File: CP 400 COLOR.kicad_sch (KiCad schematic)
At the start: 154 parts, among them CN1 CN9, CN10 CN10, CN13 CN13, CN14 CN14, CN2 CASSETE, CN3 CN8, CN4 RS232, CN5 JOYESQ, CN6 JOYDIR, CN7 CP400_CN7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

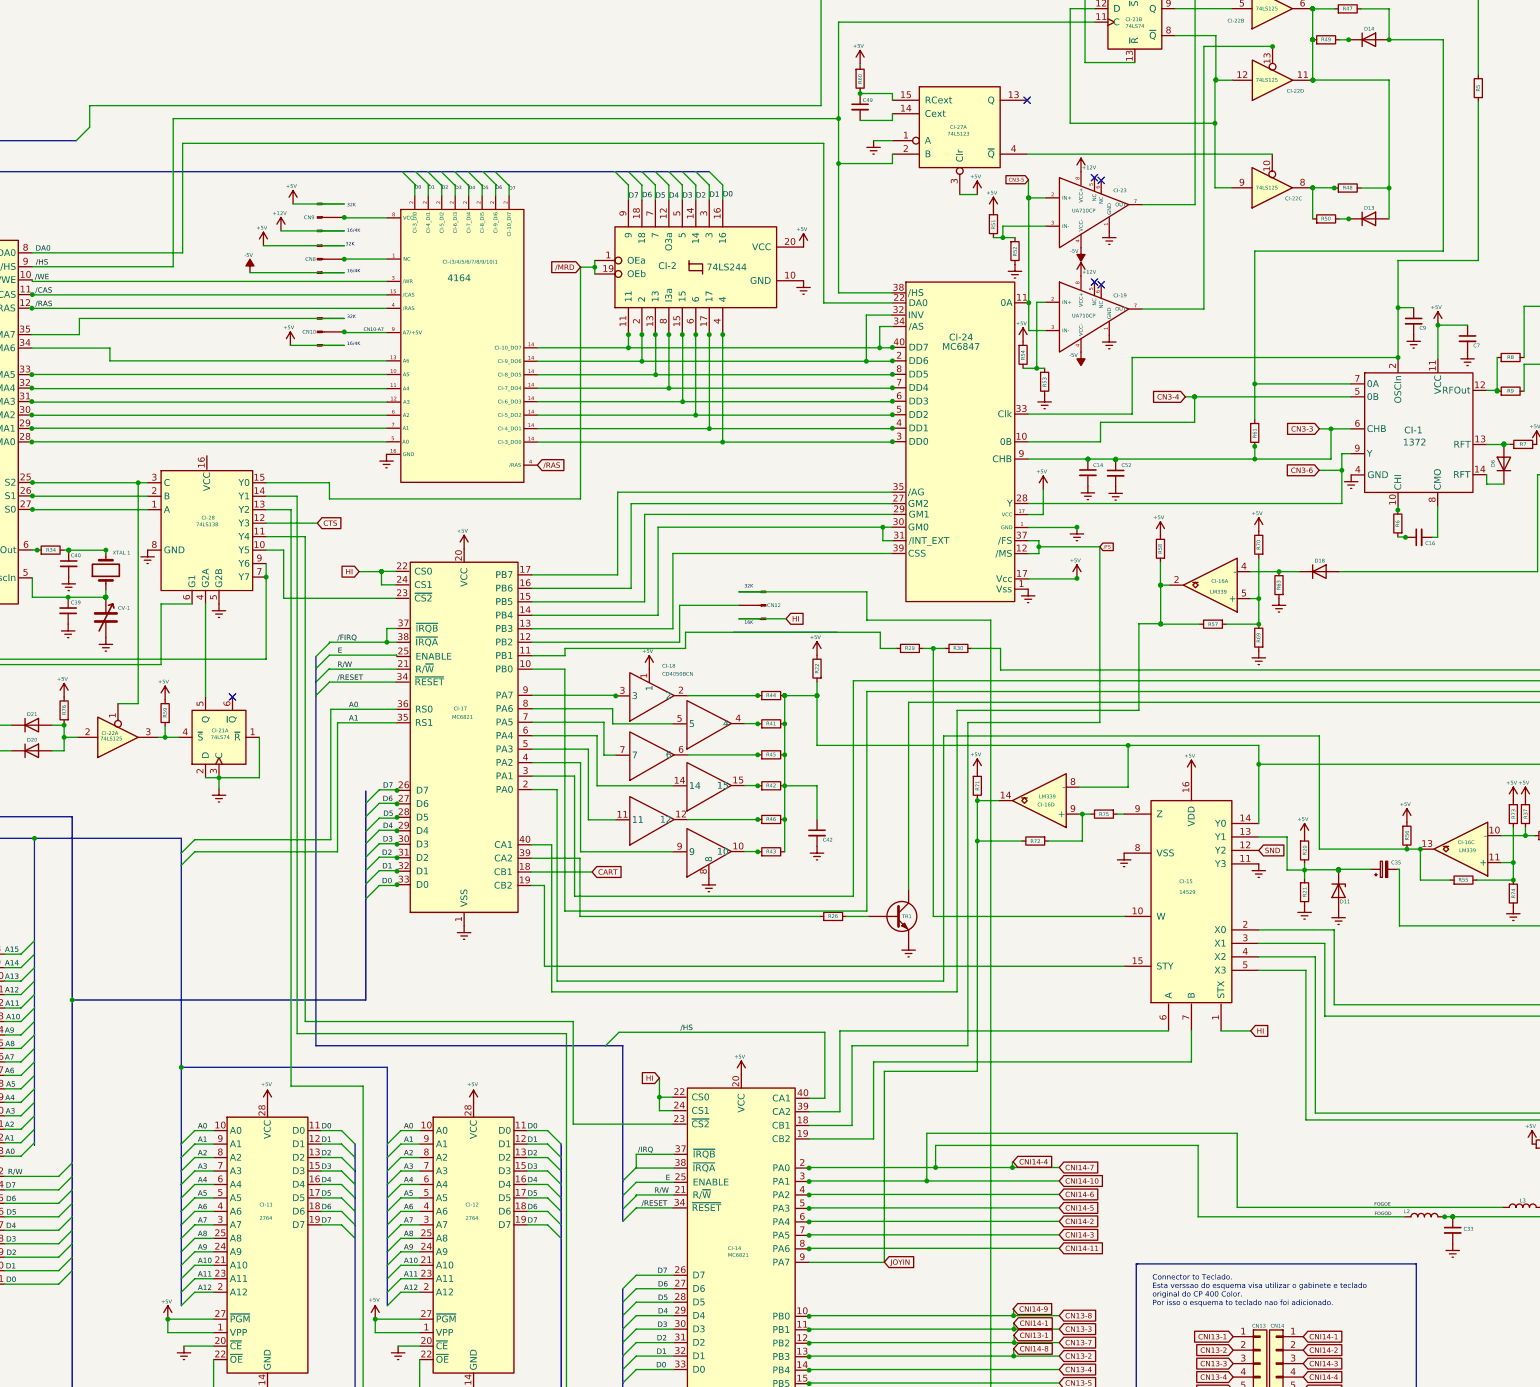
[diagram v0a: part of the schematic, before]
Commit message: Fixed VCLK signal not connected to MC1372P
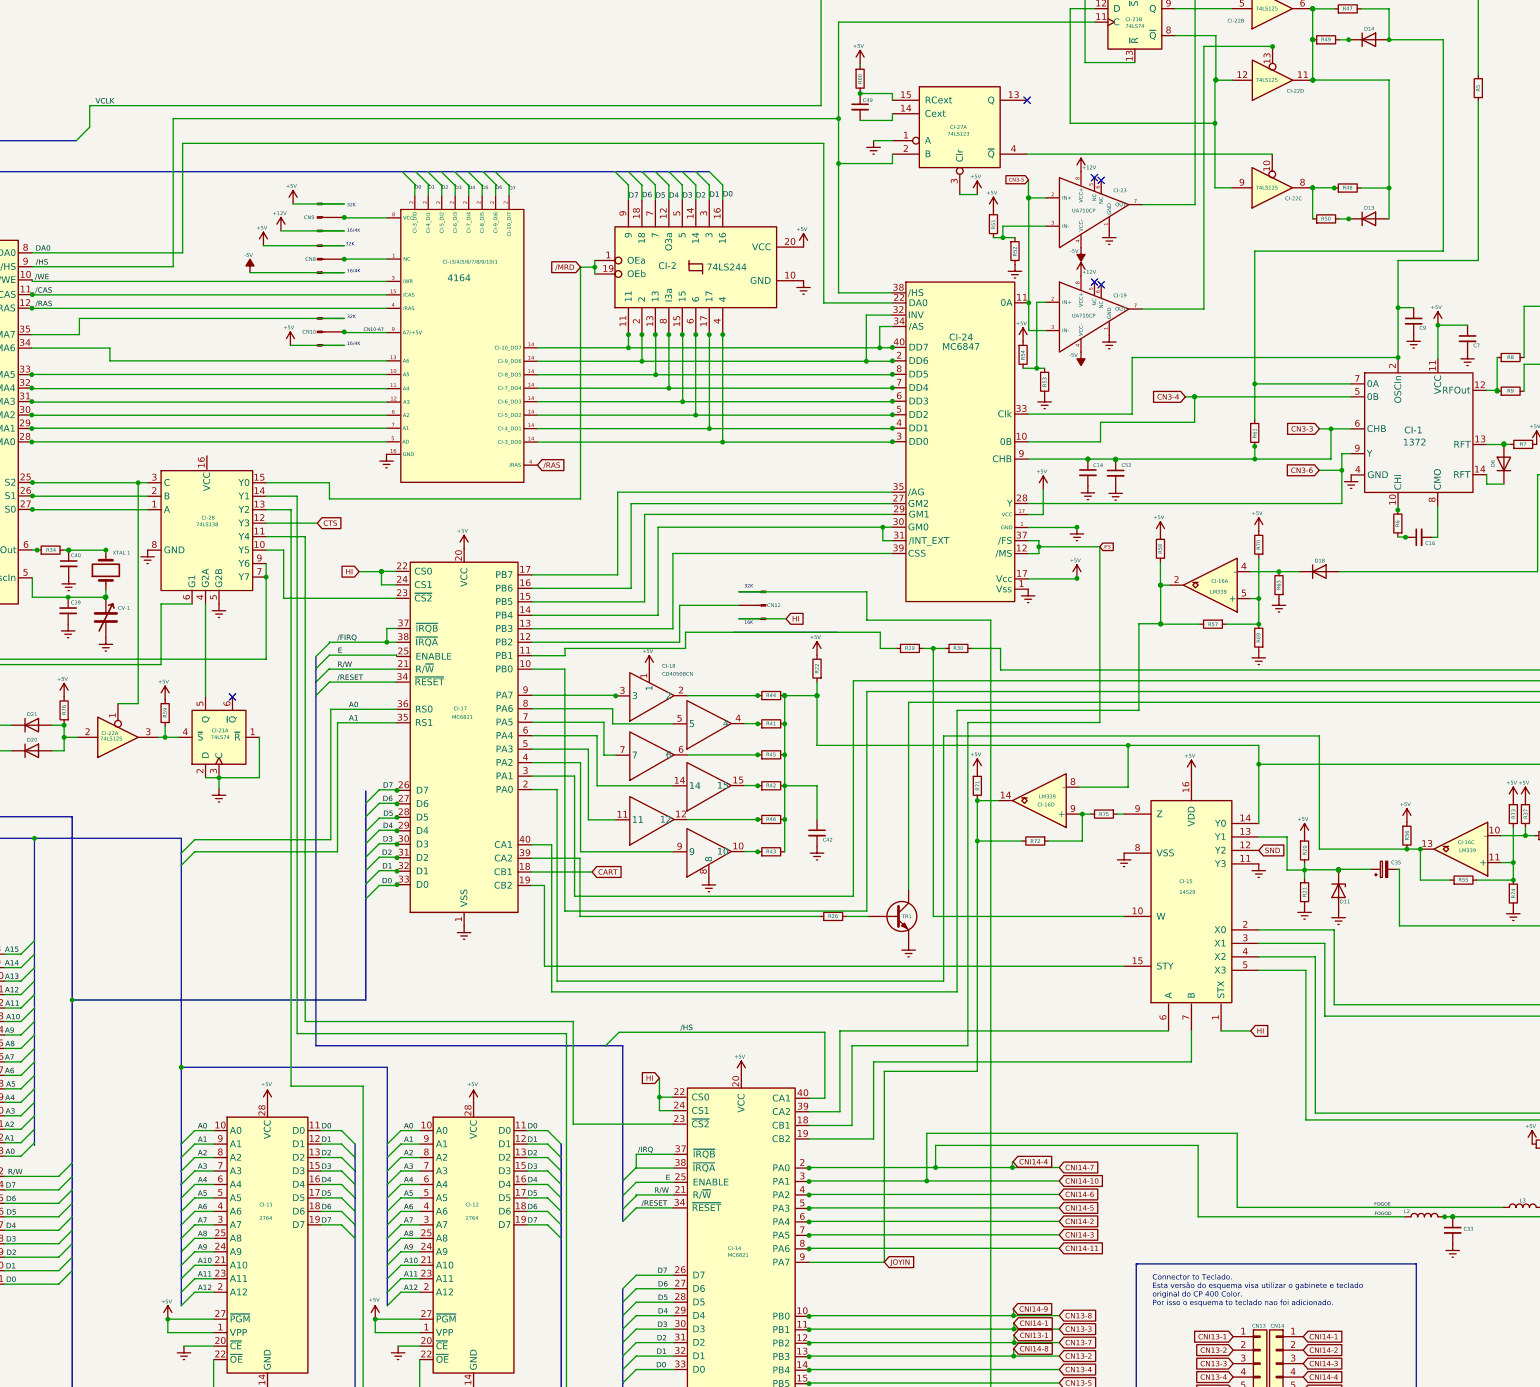
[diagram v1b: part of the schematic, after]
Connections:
- net VCLK: now also R5.2
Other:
- note added: "Connector to Teclado. Esta versão do esquema visa utilizar o gabinete e teclado original do CP 400 Color. Por isso o esquema to teclado nao foi adicionado."
- note removed: "Connector to Teclado. Esta verssao do esquema visa utilizar o gabinete e teclado original do CP 400 Color. Por isso o esquema to teclado nao foi adicionado."
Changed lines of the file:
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@@
   (title_block
     (title "CP 400 COLOR 2 - PROLOGICA 12 REV.3")
-    (date "2022-12-09")
+    (date "2022-12-13")
     (rev "0.3")
     (company "PROLOGICA")
@@
     (effects (font (size 0.635 0.635)) (justify left bottom))
   )
-  (text "Connector to Teclado.\nEsta verssao do esquema visa utilizar o gabinete e teclado \noriginal do CP 400 Color.\nPor isso o esquema to teclado nao foi adicionado."
+  (text "Connector to Teclado.\nEsta versão do esquema visa utilizar o gabinete e teclado \noriginal do CP 400 Color.\nPor isso o esquema to teclado nao foi adicionado."
     (at 359.918 279.4 0)
     (effects (font (size 1 1)) (justify left bottom))
@@
     (effects (font (size 1 1)) (justify left bottom))
   )
+  (label "VCLK" (at 160.5949 52.832 0)
+    (effects (font (size 1 1)) (justify left bottom))
+  )

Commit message: Added some component values, in what is promised to be a huge work ahead
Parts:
- removed C7: C7, Capacitor_THT:C_Disc_D3.0mm_W1.6mm_P2.50mm, symbol Device:C_Small
- added C7: 100uF, Capacitor_THT:CP_Radial_Tantal_D10.5mm_P5.00mm, symbol Device:C_Polarized_Small
- C15: value C16 -> 104
- C9: value C9 -> 560pF
- D6: value D6 -> 1N4002
- R5: value R5 -> 470
- R7: value R7 -> 360
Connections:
- net +5V: now also C7.1
- net GNDREF: now also C7.2

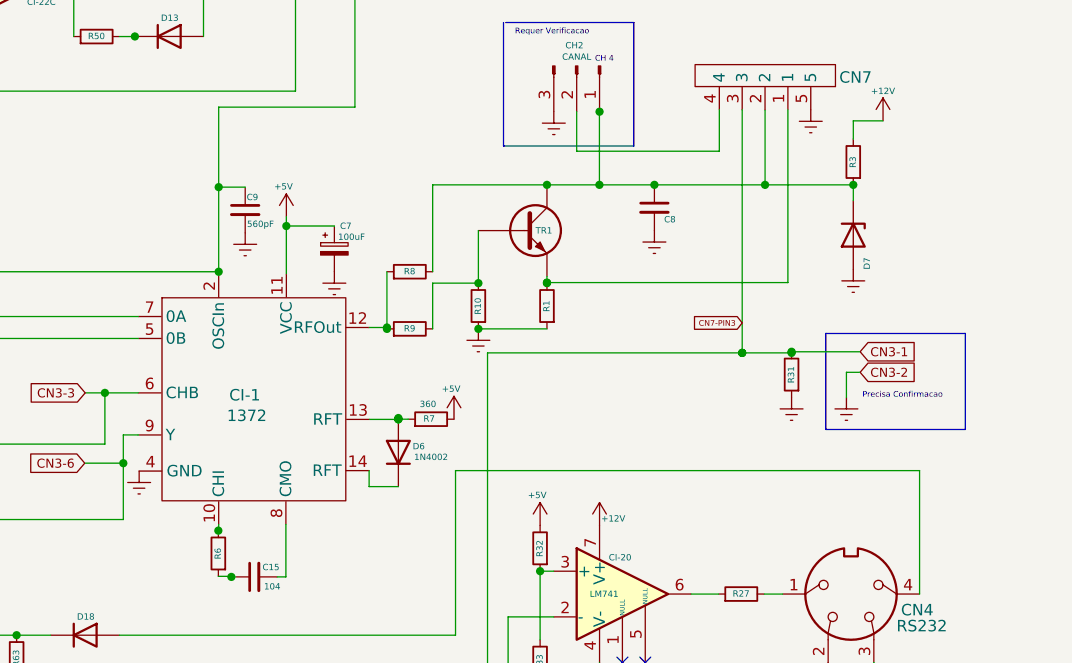
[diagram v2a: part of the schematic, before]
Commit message: Updates to some more component values; added an C8b that was not in the schematic
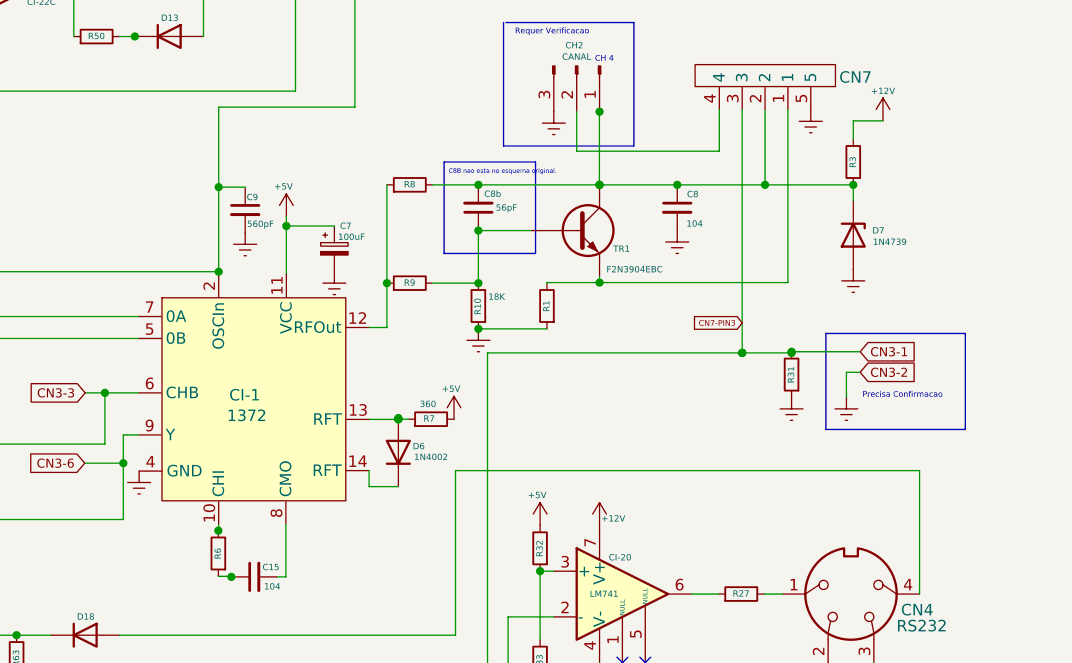
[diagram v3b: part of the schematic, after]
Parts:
- added C8b: 56pF, Capacitor_THT:C_Disc_D3.0mm_W1.6mm_P2.50mm, symbol Device:C_Small
- C8: value C8 -> 104
- D7: value D7 -> 1N4739
- R10: value R10 -> 18K
- TR1: value TR1 -> F2N3904EBC
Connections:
- net at C8.1, CH2.1 (Pin_1), CN7.2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: now also C8b.2
- net at R10.2, R9.2, TR1.2 (B): now also C8b.1
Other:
- note added: "C8B nao esta no esquema original."

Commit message: Added some components values; Added Photo with component identification in the PCB - WIP
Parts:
- C39: value C39 -> 220
- C40: value C40 -> 220
- C44: value C44 -> 1Uf 100V; footprint Capacitor_THT:CP_Radial_Tantal_D10.5mm_P5.00mm -> Capacitor_THT:CP_Axial_L10.0mm_D4.5mm_P15.00mm_Horizontal
- C45: value C45 -> 104
- C49: value C49 -> 152
- CI-(3/4/5/6/7/8/9/10)1: now left out of the parts list
- CI-23: footprint Package_DIP:DIP-8-N7_W7.62mm -> Package_DIP:DIP-8_W7.62mm
- D13: value D13 -> 1N4148
- D14: value D14 -> 1N4148
- D15: value D15 -> 1N4148
- D16: value D16 -> 1N4148
- D17: value D17 -> 1N4148
- D20: value D20 -> 1N4148
- D21: value D21 -> 1N4148
- R34: value R34 -> 1.5K
- R35: value R35 -> 100K
- R36: value R36 -> 100K
- R47: value R47 -> 9.1K 1%; footprint Resistor_THT:R_Axial_DIN0207_L6.3mm_D2.5mm_P7.62mm_Horizontal -> Resistor_THT:R_Axial_DIN0207_L6.3mm_D2.5mm_P5.08mm_Vertical
- R48: value R48 -> 7.5K; footprint Resistor_THT:R_Axial_DIN0207_L6.3mm_D2.5mm_P7.62mm_Horizontal -> Resistor_THT:R_Axial_DIN0207_L6.3mm_D2.5mm_P5.08mm_Vertical
- R49: value R49 -> 4.7K; footprint Resistor_THT:R_Axial_DIN0207_L6.3mm_D2.5mm_P7.62mm_Horizontal -> Resistor_THT:R_Axial_DIN0207_L6.3mm_D2.5mm_P5.08mm_Vertical
- R50: value R50 -> 1.2K; footprint Resistor_THT:R_Axial_DIN0207_L6.3mm_D2.5mm_P7.62mm_Horizontal -> Resistor_THT:R_Axial_DIN0207_L6.3mm_D2.5mm_P5.08mm_Vertical
- R51, R52, R53, R54: footprint Resistor_THT:R_Axial_DIN0207_L6.3mm_D2.5mm_P7.62mm_Horizontal -> Resistor_THT:R_Axial_DIN0207_L6.3mm_D2.5mm_P5.08mm_Vertical
- R59: value R59 -> 4.7K; footprint Resistor_THT:R_Axial_DIN0207_L6.3mm_D2.5mm_P7.62mm_Horizontal -> Resistor_THT:R_Axial_DIN0207_L6.3mm_D2.5mm_P5.08mm_Vertical
- R60: value R60 -> 3.3K; footprint Resistor_THT:R_Axial_DIN0207_L6.3mm_D2.5mm_P7.62mm_Horizontal -> Resistor_THT:R_Axial_DIN0207_L6.3mm_D2.5mm_P5.08mm_Vertical
- R76: value R76 -> 10K; footprint Resistor_THT:R_Axial_DIN0207_L6.3mm_D2.5mm_P7.62mm_Horizontal -> Resistor_THT:R_Axial_DIN0207_L6.3mm_D2.5mm_P5.08mm_Vertical
- XTAL1: value XTAL 1 -> 14,30244 Mhz
- renumbered C8b to C8b1
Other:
- note added: "R47 Precisa Confirmacao"

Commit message: Updated PCB component layout (photography)
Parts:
- added C10: 104, Capacitor_THT:C_Disc_D3.0mm_W1.6mm_P2.50mm, symbol Device:C_Small
- C1: value C1 -> 223
- C35: value C35 -> 10uf 25v
- C36: value C36 -> 222
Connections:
- net +5V: now also CI-28.16 (VCC), C10.1
- net GNDREF: now also C10.2
- net at C35.1, D11.1 (K): now also CI-15.13 (Y1), R20.2, R21.1
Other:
- note added: "Added in Rev 3"
- note added: "Removido no PCB Rev3"
- note added: "Reset Circuit"
- moved on the sheet: CI-27C

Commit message: .
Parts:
- R47: value 9.1K 1% -> R47
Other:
- note added: "C8b1 nao esta no esquema original."
- note removed: "C8B nao esta no esquema original."
- note removed: "R47 Precisa Confirmacao"
- moved on the sheet: CI-2
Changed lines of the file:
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@@
     (effects (font (size 0.635 0.635)) (justify left bottom))
   )
-  (text "RESET signal \nfrom Keyboard\n" (at 105.41 156.972 0)
+  (text "RESET signal \nfrom Keyboard\n" (at 106.68 157.226 0)
     (effects (font (size 0.635 0.635)) (justify left bottom))
   )
@@
     (effects (font (size 0.635 0.635)) (justify left bottom))
   )
-  (text "C8B nao esta no esquema original." (at 431.8 89.662 0)
+  (text "C8b1 nao esta no esquema original." (at 431.8 89.662 0)
     (effects (font (size 0.5 0.5)) (justify left bottom))
   )
@@
     (effects (font (size 0.635 0.635)) (justify left bottom))
   )
-  (text "R47\nPrecisa Confirmacao" (at 392.684 33.274 0)
-    (effects (font (size 0.635 0.635)) (justify left bottom))
-  )
   (text "Precisa Confirmacao" (at 477.774 114.554 0)
     (effects (font (size 0.635 0.635)) (justify left bottom))
@@
     (pin "3")
   )
-  (symbol (lib_id "power:GNDREF") (at 294.132 85.852 0) (unit 1)
+  (symbol (lib_id "power:GNDREF") (at 287.274 85.852 0) (unit 1)
     (in_bom yes) (on_board yes) (fields_autoplaced)
-    (property "Reference" "#PWR02" (id 0) (at 294.132 92.202 0)
+    (property "Reference" "#PWR02" (id 0) (at 287.274 92.202 0)
       (effects (font (size 0.7 0.7)) hide)
     )
-    (property "Value" "GNDREF" (id 1) (at 294.132 90.424 0)
+    (property "Value" "GNDREF" (id 1) (at 287.274 90.424 0)
       (effects (font (size 0.7 0.7)) hide)
     )
-    (property "Footprint" "" (id 2) (at 294.132 85.852 0)
+    (property "Footprint" "" (id 2) (at 287.274 85.852 0)
       (effects (font (size 0.7 0.7)) hide)
     )
-    (property "Datasheet" "" (id 3) (at 294.132 85.852 0)
+    (property "Datasheet" "" (id 3) (at 287.274 85.852 0)
       (effects (font (size 0.7 0.7)) hide)
     )
@@
       (effects (font (size 0.7 0.7)) (justify left))
     )
-    (property "Value" "9.1K 1%" (id 1) (at 396.748 36.068 90)
+    (property "Value" "R47" (id 1) (at 396.748 36.068 90)
       (effects (font (size 0.7 0.7)))
     )
@@
     (pin "7")
   )
-  (symbol (lib_id "power:+5V") (at 294.132 79.502 0) (unit 1)
+  (symbol (lib_id "power:+5V") (at 287.274 79.502 0) (unit 1)
     (in_bom yes) (on_board yes)
-    (property "Reference" "#PWR01" (id 0) (at 294.132 83.312 0)
+    (property "Reference" "#PWR01" (id 0) (at 287.274 83.312 0)
       (effects (font (size 0.7 0.7)) hide)
     )
-    (property "Value" "+5V" (id 1) (at 293.8145 76.1369 0)
+    (property "Value" "+5V" (id 1) (at 286.9565 76.1369 0)
       (effects (font (size 0.7 0.7)))
     )
-    (property "Footprint" "" (id 2) (at 294.132 79.502 0)
+    (property "Footprint" "" (id 2) (at 287.274 79.502 0)
       (effects (font (size 0.7 0.7)) hide)
     )
-    (property "Datasheet" "" (id 3) (at 294.132 79.502 0)
+    (property "Datasheet" "" (id 3) (at 287.274 79.502 0)
       (effects (font (size 0.7 0.7)) hide)
     )
@@
   (symbol (lib_id "Roni:CP400_74LS244") (at 273.812 83.312 90) (unit 1)
     (in_bom yes) (on_board yes)
-    (property "Reference" "CI-2" (id 0) (at 268.478 83.058 90))
-    (property "Value" "74LS244" (id 1) (at 279.654 83.312 90))
+    (property "Reference" "CI-2" (id 0) (at 269.494 81.534 90)
+      (effects (font (size 1 1)))
+    )
+    (property "Value" "74LS244" (id 1) (at 268.986 83.312 90)
+      (effects (font (size 1 1)))
+    )
     (property "Footprint" "Package_DIP:DIP-20_W7.62mm" (id 2) (at 273.812 83.312 0)
       (effects (font (size 1.27 1.27)) hide)
@@
     )
     (path "/293bb476-09a1-45bb-8b16-3248945a44ac"
-      (reference "R47") (unit 1) (value "9.1K 1%") (footprint "Resistor_THT:R_Axial_DIN0207_L6.3mm_D2.5mm_P5.08mm_Vertical")
+      (reference "R47") (unit 1) (value "R47") (footprint "Resistor_THT:R_Axial_DIN0207_L6.3mm_D2.5mm_P5.08mm_Vertical")
     )
     (path "/4f55b128-5cbf-46db-a25a-4ef4d3bb4758"

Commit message: .
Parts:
- C1, C10, C12, C13, C14, C15, C2, C3, C33, C34, C36, C39, C4, C40, C42, C45, C49, C5, C52, C6, C8, C8b1, C9: footprint Capacitor_THT:C_Disc_D3.0mm_W1.6mm_P2.50mm -> Capacitor_THT:C_Axial_L3.8mm_D2.6mm_P7.50mm_Horizontal
- D12, D13, D15, D16, D17, D18, D19, D20, D21: footprint Diode_THT:D_DO-34_SOD68_P10.16mm_Horizontal -> Diode_THT:D_DO-34_SOD68_P7.62mm_Horizontal
- D14: footprint Diode_THT:D_DO-34_SOD68_P10.16mm_Horizontal -> Diode_THT:D_DO-35_SOD27_P2.54mm_Vertical_AnodeUp
- R22, R41, R42, R43, R44, R45, R46: footprint Resistor_THT:R_Axial_DIN0207_L6.3mm_D2.5mm_P7.62mm_Horizontal -> Resistor_THT:R_Axial_DIN0207_L6.3mm_D2.5mm_P2.54mm_Vertical
- R47, R48, R49, R50, R51, R52, R53, R54, R59, R60, R76: footprint Resistor_THT:R_Axial_DIN0207_L6.3mm_D2.5mm_P5.08mm_Vertical -> Resistor_THT:R_Axial_DIN0207_L6.3mm_D2.5mm_P2.54mm_Vertical
